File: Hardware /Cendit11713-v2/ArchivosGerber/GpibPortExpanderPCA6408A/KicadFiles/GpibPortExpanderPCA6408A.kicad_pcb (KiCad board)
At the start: 2 copper layers, 30 parts, among them P1 CONN_01X07, U1 PCA6408A, U2 PCA6408A

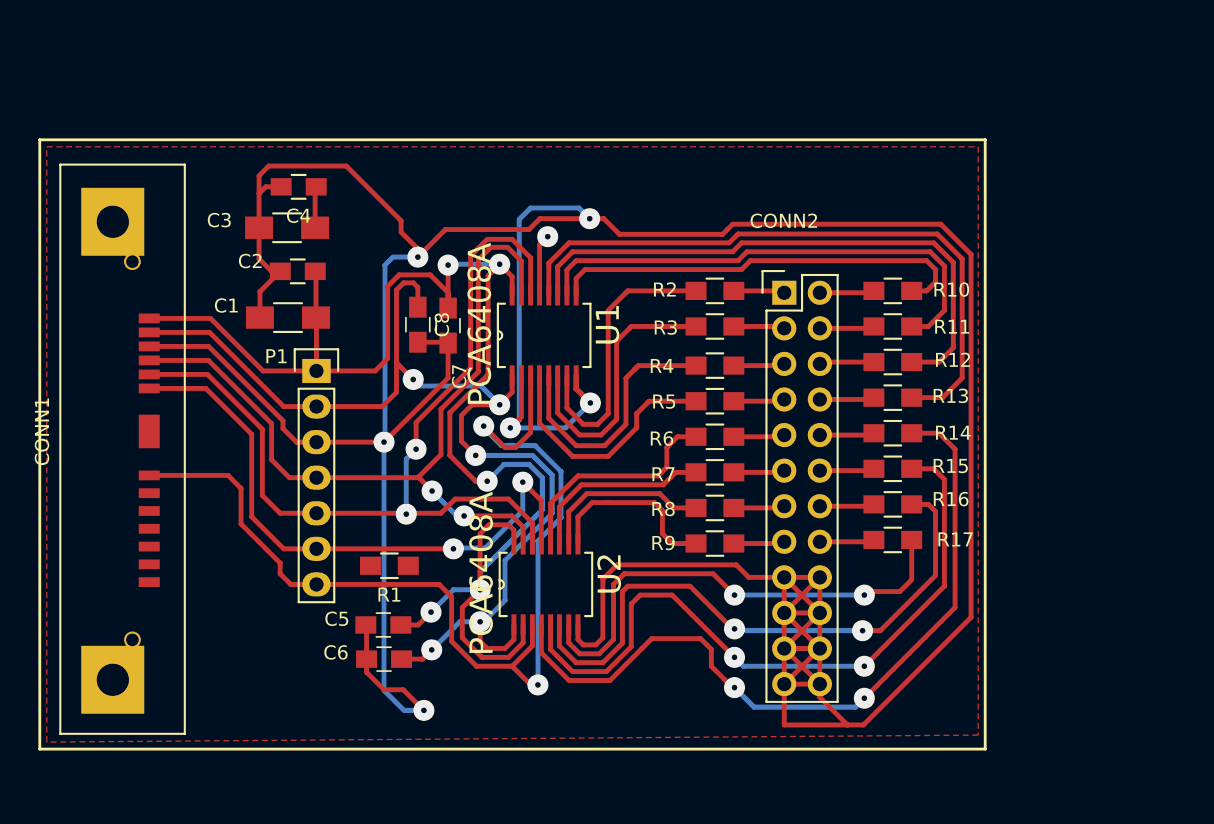
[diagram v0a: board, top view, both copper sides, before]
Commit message: En Cendit11713 + respaldo de software
  - Esquematico tarjeta madre con PIC18F45K50
  - Respaldo de software CenditLab
  - Gerber files tarjeta interfaz GPIB
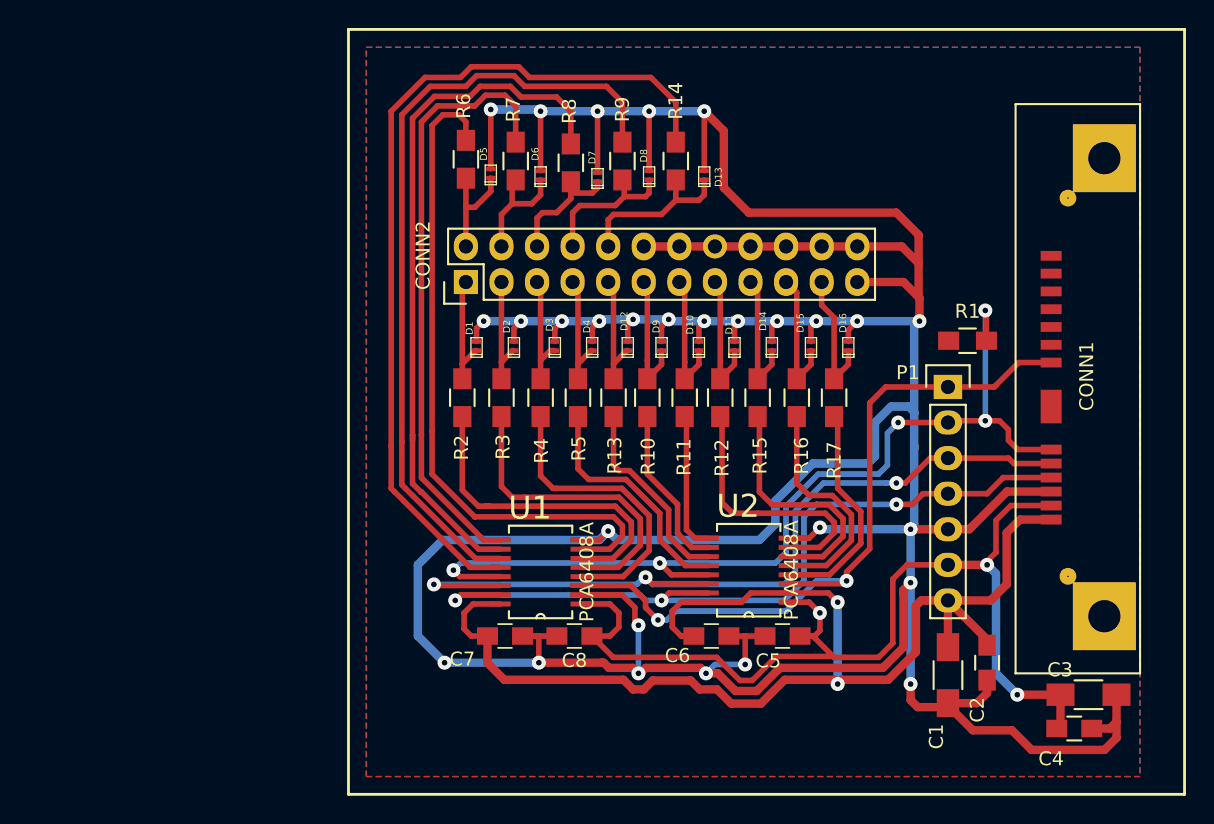
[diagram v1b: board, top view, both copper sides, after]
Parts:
- added D1: SPHV24, CenditFootprints:SPHV24-SOD882, F.Cu at (138.7, 93.7)
- added D10: SPHV24, CenditFootprints:SPHV24-SOD882, F.Cu at (154.6, 93.7)
- added D11: SPHV24, CenditFootprints:SPHV24-SOD882, F.Cu at (157.1, 93.7)
- added D12: SPHV24, CenditFootprints:SPHV24-SOD882, F.Cu at (149.5, 93.7)
- added D13: SPHV24, CenditFootprints:SPHV24-SOD882, F.Cu at (154.9, 81.5)
- added D14: SPHV24, CenditFootprints:SPHV24-SOD882, F.Cu at (159.8, 93.7)
- added D15: SPHV24, CenditFootprints:SPHV24-SOD882, F.Cu at (162.6, 93.7)
- added D16: SPHV24, CenditFootprints:SPHV24-SOD882, F.Cu at (165.2, 93.7)
- added D2: SPHV24, CenditFootprints:SPHV24-SOD882, F.Cu at (141.4, 93.7)
- added D3: SPHV24, CenditFootprints:SPHV24-SOD882, F.Cu at (144.3, 93.7)
- added D4: SPHV24, CenditFootprints:SPHV24-SOD882, F.Cu at (146.9, 93.7)
- added D5: SPHV24, CenditFootprints:SPHV24-SOD882, F.Cu at (139.7, 81.4)
- added D6: SPHV24, CenditFootprints:SPHV24-SOD882, F.Cu at (143.3, 81.5)
- added D7: SPHV24, CenditFootprints:SPHV24-SOD882, F.Cu at (147.3, 81.7)
- added D8: SPHV24, CenditFootprints:SPHV24-SOD882, F.Cu at (151.0, 81.5)
- added D9: SPHV24, CenditFootprints:SPHV24-SOD882, F.Cu at (151.9, 93.7)
- CONN2: footprint Pin_Headers:Pin_Header_Straight_2x12 -> CenditFootprints:GPIB_HEADER_12X2P
- moved C4 67.5 mm to (181.4, 121.0), turned to 0 degrees
- moved C3 66.2 mm to (182.4, 118.6), turned to 0 degrees
- moved CONN1 64.4 mm to (179.7, 98.0), turned to 90 degrees
- moved C2 56.6 mm to (175.1, 116.3), turned to 270 degrees
- moved C1 53.6 mm to (172.3, 117.2), turned to 270 degrees
- moved P1 45.1 mm to (172.3, 96.6)
- moved R1 44.3 mm to (173.7, 93.3), turned to 0 degrees
- moved C6 28.5 mm to (160.5, 114.4)
- moved R9 28.1 mm to (149.1, 80.5), turned to 90 degrees
- moved R8 26.7 mm to (145.4, 80.6), turned to 90 degrees
- moved R6 26.6 mm to (137.9, 80.4), turned to 90 degrees
- moved R7 26.4 mm to (141.5, 80.5), turned to 90 degrees
- moved C8 24.9 mm to (145.7, 114.4), turned to 180 degrees
- moved R14 24.9 mm to (152.9, 80.5), turned to 90 degrees
- moved C5 23.4 mm to (155.4, 114.4), turned to 0 degrees
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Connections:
- CONN2 pad 10: /IFC -> /REN
- CONN2 pad 11: /D5 -> /DAV
- CONN2 pad 12: /REN -> GNDD
- CONN2 pad 13: /D6 -> /NRFD
- CONN2 pad 14: /SRQ -> GNDD
- CONN2 pad 15: /D7 -> /NDAC
- CONN2 pad 16: /EOI -> GNDD
- CONN2 pad 17: GNDD -> /IFC
- CONN2 pad 19: GNDD -> /SRQ
- CONN2 pad 2: /NRFD -> /D4
- CONN2 pad 21: GNDD -> /ATN
- CONN2 pad 4: /NDAC -> /D5
- CONN2 pad 6: /DAV -> /D6
- CONN2 pad 8: /ATN -> /D7
- CONN2 pad 9: /D4 -> /EOI
- P1 pad 1: +5V -> //RESET
- P1 pad 2: +3V3 -> //INT
- P1 pad 3: GNDD -> /SCL
- P1 pad 5: /SCL -> GNDD
- P1 pad 6: //INT -> +3V3
- P1 pad 7: //RESET -> +5V
- R10 pad 1: /NRFD -> /DAV
- R10 pad 2: /PNRFD -> /PNDAC
- R11 pad 1: /NDAC -> /NRFD
- R11 pad 2: /PNDAC -> /PNRFD
- R12 pad 1: /DAV -> /NDAC
- R13 pad 1: /ATN -> /EOI
- R13 pad 2: /PATN -> /PEOI
- R14 pad 1: /IFC -> /REN
- R14 pad 2: /PIFC -> /PREN
- R15 pad 1: /REN -> /IFC
- R15 pad 2: /PREN -> /PIFC
- R17 pad 1: /EOI -> /ATN
- R17 pad 2: /PEOI -> /PATN
- U1 pad 10: /PNDAC -> /PD6
- U1 pad 11: /PDAV -> /PD7
- U1 pad 12: /PATN -> /PREN
- U1 pad 4: /PD3 -> /PD2
- U1 pad 5: /PD2 -> /PD1
- U1 pad 6: /PD1 -> /PD0
- U1 pad 7: /PD0 -> /PD4
- U1 pad 9: /PNRFD -> /PD5
- U2 pad 10: /PD6 -> /PNDAC
- U2 pad 11: /PD5 -> /PEOI
- U2 pad 12: /PD4 -> /PD3
- U2 pad 4: /PIFC -> /PATN
- U2 pad 5: /PREN -> /PSRQ
- U2 pad 6: /PSRQ -> /PIFC
- U2 pad 7: /PEOI -> /PDAV
- U2 pad 9: /PD7 -> /PNRFD
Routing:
- net /PD7: track 13.1 -> 56.2 mm
- net /PD6: track 12.4 -> 50.1 mm
- net /PIFC: track 54.2 -> 17.9 mm, vias 2 -> 0
- net /PD4: track 16.1 -> 48.4 mm
- net /PATN: track 46.1 -> 15.9 mm
- net /PD5: track 13.4 -> 43.3 mm
- net GNDD: track 300.6 -> 327.3 mm, vias 6 -> 28
- net /PSRQ: track 42.7 -> 16.6 mm, vias 2 -> 0
- net /PNDAC: track 35.7 -> 11.9 mm
- net /PDAV: track 41.0 -> 19.2 mm
- net //INT: track 47.4 -> 69.1 mm, vias 3 -> 5
- net /PEOI: track 34.7 -> 14.1 mm, vias 2 -> 0
- net /PNRFD: track 30.5 -> 9.96 mm
- net //RESET: track 72.8 -> 53.3 mm
- net +5V: track 105.3 -> 89.2 mm, vias 5 -> 2
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- added copper zone on B.Cu, net GNDD
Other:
- net class GND added: clearance 0.25, trace_width 0.6, via_dia 0.6, via_drill 0.4
- net class PORT added: clearance 0.2, trace_width 0.4, via_dia 1.6, via_drill 0.4
- net class POWER_3V added: clearance 0.25, trace_width 0.4, via_dia 0.6, via_drill 0.4
- net class POWER_5V added: clearance 0.25, trace_width 0.6, via_dia 1.6, via_drill 0.4

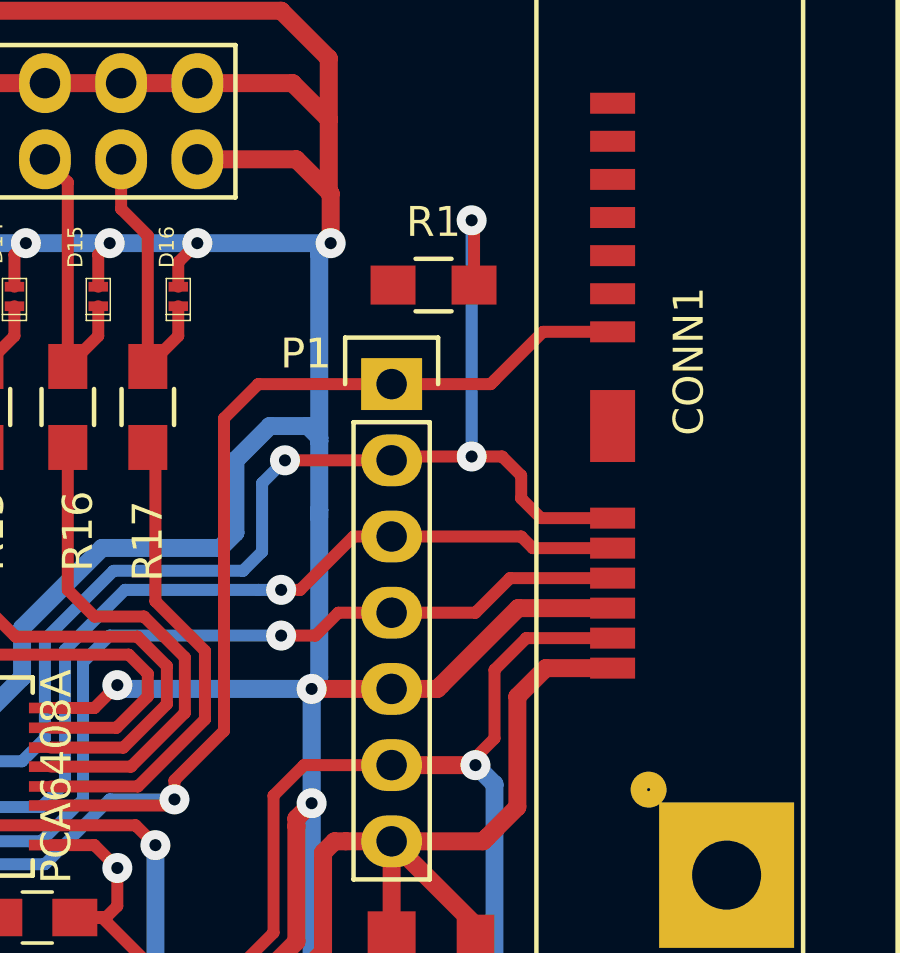
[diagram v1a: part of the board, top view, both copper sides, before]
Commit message: En Cendit11713 + CenditLab respaldo
  - Se revisan tarjetas
  - Correccion en PCB GPIB
  - Se inicia tarjeta madre en una pieza (MainBoard.OnePiece)
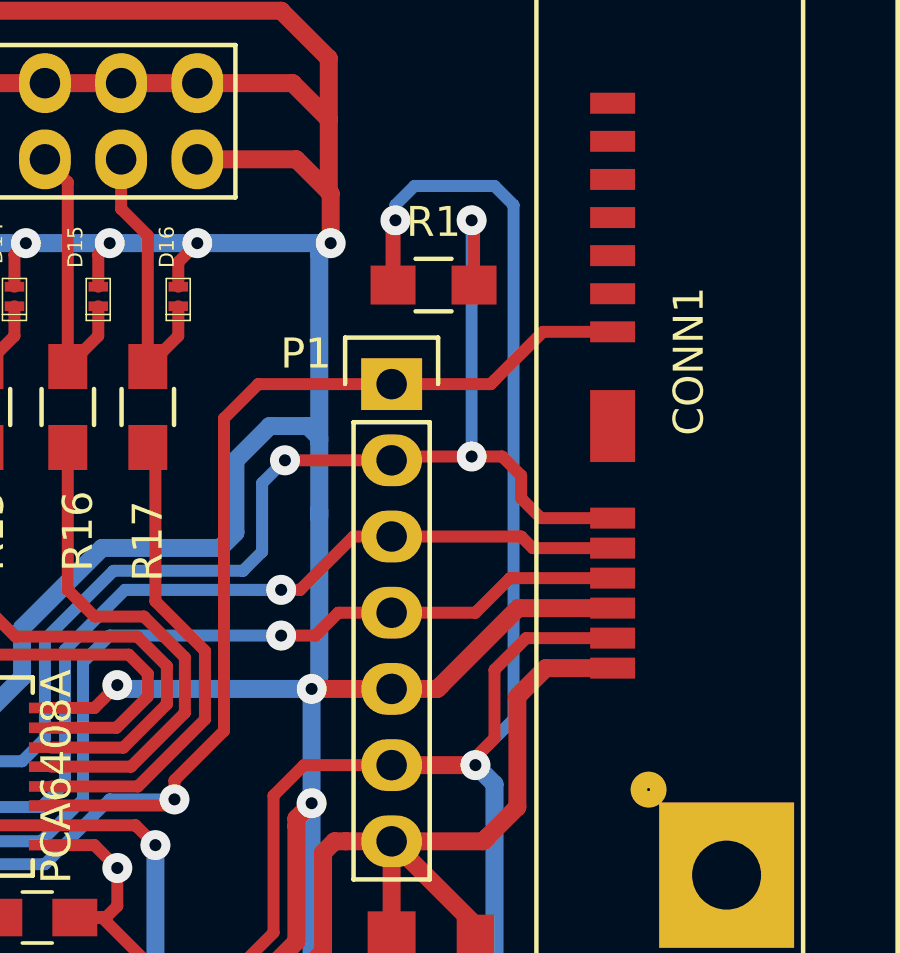
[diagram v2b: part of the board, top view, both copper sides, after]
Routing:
- net +3V3: track 74.0 -> 100.1 mm, vias 3 -> 4
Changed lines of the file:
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@@
-(kicad_pcb (version 4) (host pcbnew 4.0.5+dfsg1-4~bpo8+1)
+(kicad_pcb (version 4) (host pcbnew 4.0.6-e0-6349~53~ubuntu14.04.1)
   (general
     (links 113)
-    (no_connects 1)
-    (area 129.439999 71.019999 189.330001 125.830001)
+    (no_connects 0)
+    (area 129.439999 71.019999 203.493572 137.320001)
     (thickness 1.6)
     (drawings 6)
-    (tracks 606)
+    (tracks 615)
     (zones 0)
     (modules 46)
@@
   (page A4)
   (layers
-    (0 F.Cu signal)
+    (0 F.Cu signal hide)
     (31 B.Cu signal)
     (32 B.Adhes user)
@@
   )
   (setup
-    (last_trace_width 0.25)
+    (last_trace_width 0.4)
     (user_trace_width 0.3)
     (user_trace_width 0.325)
@@
       (padsonsilk false)
       (subtractmaskfromsilk false)
-      (outputformat 1)
+      (outputformat 4)
       (mirror false)
       (drillshape 0)
       (scaleselection 1)
-      (outputdirectory "/home/jarias/Escritorio/Pasantia/Desarrollo/Hardware /Cendit11713-v2/GpibPortExpanderPCA6408A/"))
+      (outputdirectory "/home/jarias/Escritorio/Pasantia/Desarrollo/Hardware /Cendit11713-v2/ArchivosGerber/GpibPortExpanderPCA6408A/GerberFiles/"))
   )
   (net 0 "")
@@
   (segment (start 142.748 114.427) (end 143.129 114.427) (width 0.4) (layer F.Cu) (net 2))
   (segment (start 143.129 114.427) (end 144.419 114.427) (width 0.4) (layer F.Cu) (net 2))
+  (segment (start 175.133 109.347) (end 175.133 109.093) (width 0.5) (layer B.Cu) (net 3))
+  (segment (start 175.133 109.093) (end 176.403 107.823) (width 0.4) (layer B.Cu) (net 3))
+  (segment (start 172.386 91.266) (end 172.466 91.186) (width 0.5) (layer F.Cu) (net 3))
+  (via (at 172.466 91.186) (size 1) (drill 0.4) (layers F.Cu B.Cu) (net 3))
+  (segment (start 172.386 93.345) (end 172.386 91.266) (width 0.5) (layer F.Cu) (net 3) (status 400000))
+  (segment (start 172.466 90.678) (end 172.466 91.186) (width 0.4) (layer B.Cu) (net 3))
+  (segment (start 173.101 90.043) (end 172.466 90.678) (width 0.4) (layer B.Cu) (net 3))
+  (segment (start 175.768 90.043) (end 173.101 90.043) (width 0.4) (layer B.Cu) (net 3))
+  (segment (start 176.403 90.678) (end 175.768 90.043) (width 0.4) (layer B.Cu) (net 3))
+  (segment (start 176.403 107.823) (end 176.403 90.678) (width 0.4) (layer B.Cu) (net 3))
   (segment (start 180.372 118.618) (end 180.372 120.765) (width 0.6) (layer F.Cu) (net 3))
   (segment (start 180.372 120.765) (end 180.106 121.031) (width 0.4) (layer F.Cu) (net 3))
@@
   (segment (start 175.768 117.094) (end 177.292 118.618) (width 0.6) (layer B.Cu) (net 3))
   (segment (start 175.768 109.982) (end 175.768 117.094) (width 0.6) (layer B.Cu) (net 3))
-  (segment (start 175.133 109.347) (end 175.133 109.093) (width 0.4) (layer F.Cu) (net 3))
   (segment (start 175.768 108.458) (end 175.768 106.172) (width 0.4) (layer F.Cu) (net 3))
   (segment (start 176.826 105.114) (end 179.705 105.114) (width 0.4) (layer F.Cu) (net 3))
